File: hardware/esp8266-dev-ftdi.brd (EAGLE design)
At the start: 50 x 50 mm, 58 parts, among them CON1 USBMICRO-NO_CENTER-LONG_PADS

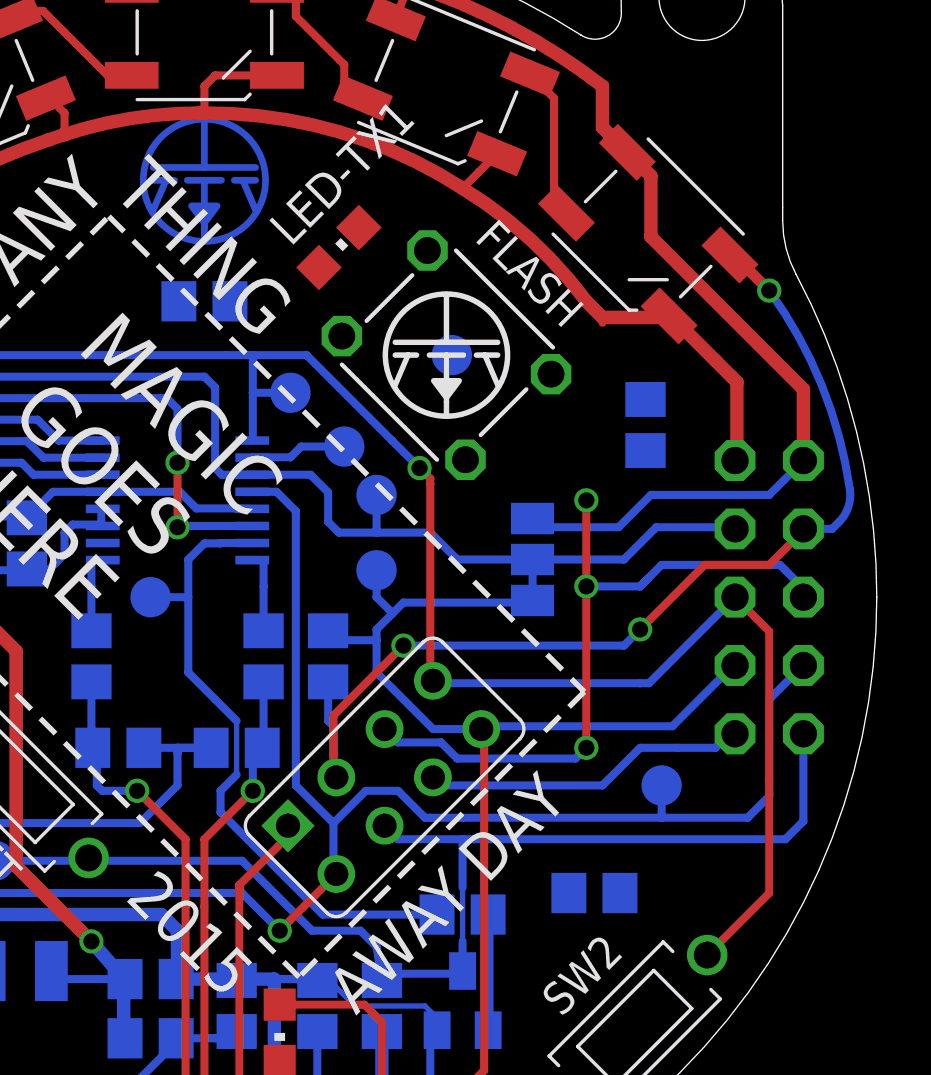
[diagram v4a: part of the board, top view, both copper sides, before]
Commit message: routed new components in layout
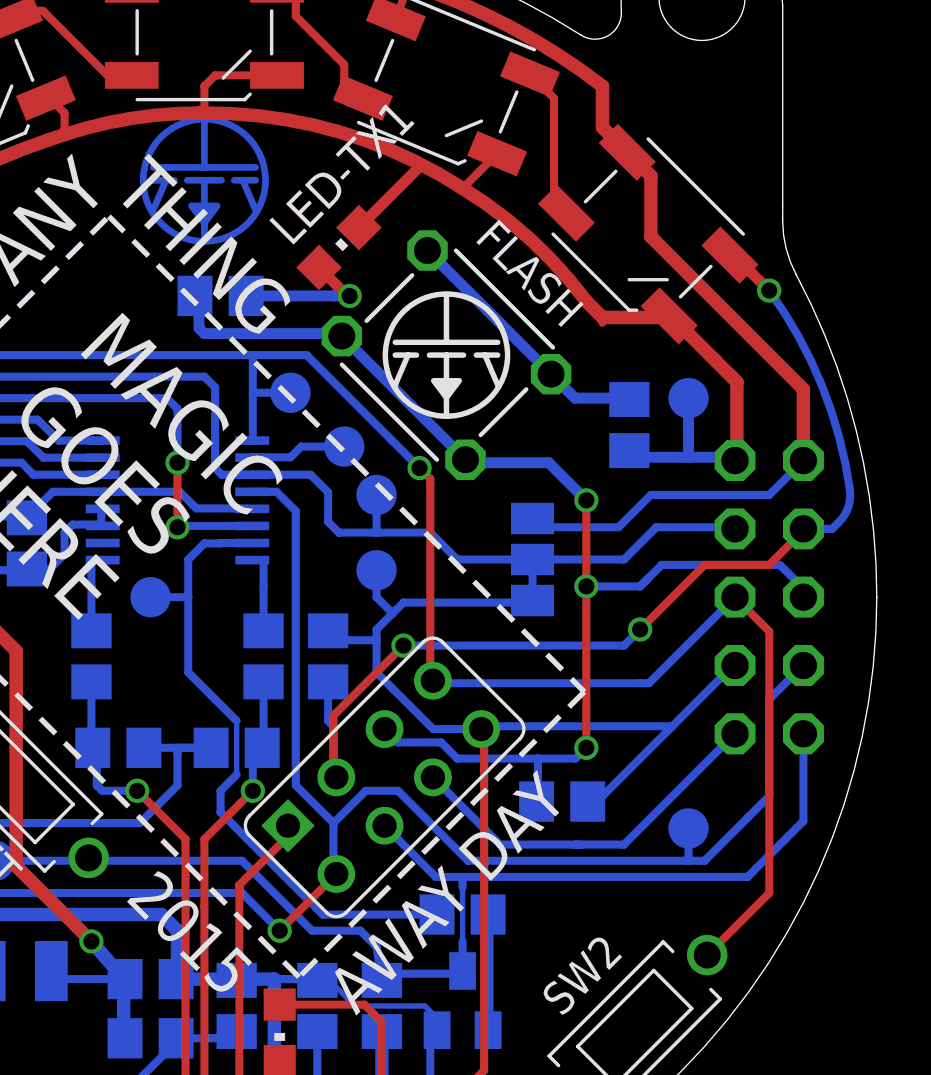
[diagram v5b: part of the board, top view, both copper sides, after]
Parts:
- moved GND 8.94 mm to (43.0, 32.4)
- moved R12 3.61 mm to (38.3, 17.4)
- moved RX 1.89 mm to (43.0, 16.4)
- moved R13 0.63 mm to (25.6, 36.2), turned to 0 degrees
- moved R7 0.60 mm to (40.8, 31.4)
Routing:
- net IO0: track 26.8 -> 46.7 mm
- net GND: track 189.2 -> 200.8 mm
- net N$11: track 0.00 -> 9.79 mm
- net N$22: track 0.00 -> 5.43 mm, vias 0 -> 1
- net +3V3: track 84.8 -> 89.1 mm
- net IO16: track 12.2 -> 14.3 mm
- net RX: track 79.6 -> 80.9 mm
